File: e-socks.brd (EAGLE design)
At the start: 65.1 x 30 mm, 93 parts, among them IC1 CC2540, IC2 741G240DCK, Q1 FA-20H(32MHz), Q2 ABS06, U2 MAX21000, X4 1296-T10

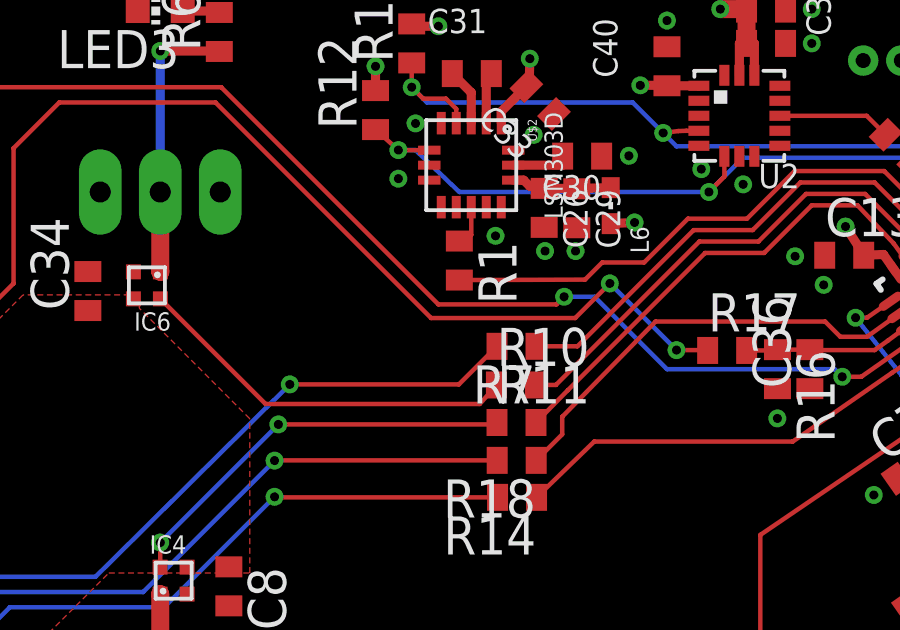
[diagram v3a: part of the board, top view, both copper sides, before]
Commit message: 4K Pulldown Widerstand hinzugefügt, um den Pullup Widerstand im Reset zu überstimmen (nur für 5V-Enable), einige Widerstandswerte angepasst)
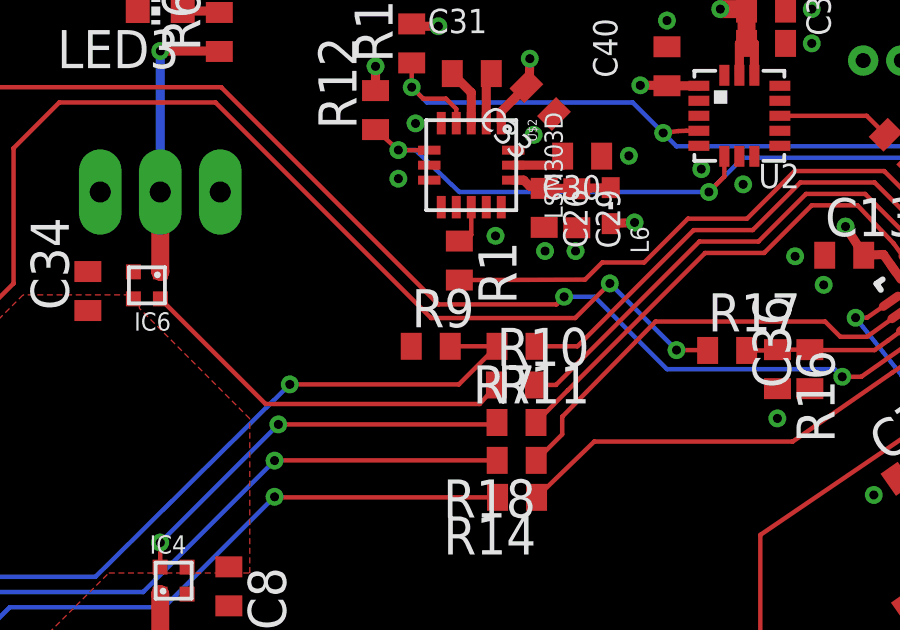
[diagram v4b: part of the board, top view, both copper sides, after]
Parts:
- added R9: 4K, rcl:R0402
- C11: value 100nF -> 220nF
- R16: value 10K -> 24K
- R19: value 4K7 -> 1K2
- R20: value 4K7k -> 1k
- R3: value 47R -> 100k
- R5: value 47R -> 360k
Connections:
- net 5V_ENABLE: now also R9.2
- net GND: now also R9.1
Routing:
- net 5V_ENABLE: track 30.9 -> 32.5 mm
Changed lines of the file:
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@@
 <layer number="20" name="Dimension" color="15" fill="1" visible="yes" active="yes"/>
 <layer number="21" name="tPlace" color="7" fill="1" visible="yes" active="yes"/>
-<layer number="22" name="bPlace" color="7" fill="1" visible="yes" active="yes"/>
+<layer number="22" name="bPlace" color="7" fill="1" visible="no" active="yes"/>
 <layer number="23" name="tOrigins" color="15" fill="1" visible="yes" active="yes"/>
 <layer number="24" name="bOrigins" color="15" fill="1" visible="yes" active="yes"/>
@@
 <element name="R21" library="rcl" package="R0402" value="150K" x="13.02675" y="20.34325" rot="R90"/>
 <element name="R22" library="rcl" package="R0402" value="430K" x="11.88575" y="20.379" rot="R270"/>
-<element name="C11" library="rcl" package="C0402" value="100nF" x="12.016" y="28.0055" rot="R270"/>
-<element name="R20" library="rcl" package="R0402" value="4K7k" x="10.81875" y="28.1405" rot="R90"/>
-<element name="R19" library="rcl" package="R0402" value="4K7" x="9.689" y="27.97925" rot="R90"/>
+<element name="C11" library="rcl" package="C0402" value="220nF" x="12.016" y="28.0055" rot="R270"/>
+<element name="R20" library="rcl" package="R0402" value="1k" x="10.81875" y="28.1405" rot="R90"/>
+<element name="R19" library="rcl" package="R0402" value="1K2" x="9.689" y="27.97925" rot="R90"/>
 <element name="C20" library="resistor" package="C0402" value="2,2µF" x="9.898" y="20.74225" rot="R180"/>
 <element name="R4" library="rcl" package="R0402" value="220R" x="2.555" y="24.06375" rot="MR180"/>
@@
 <element name="R14" library="rcl" package="R0402" value="220R" x="32.784596875" y="12.8719" rot="R180"/>
 <element name="R15" library="rcl" package="R0402" value="47R" x="9.162596875" y="2.17759375"/>
-<element name="R16" library="rcl" package="R0402" value="10K" x="41.4655" y="17.145" rot="R270"/>
+<element name="R16" library="rcl" package="R0402" value="24K" x="41.4655" y="17.145" rot="R270"/>
 <element name="R17" library="rcl" package="R0402" value="10K" x="39.788196875" y="17.76910625"/>
 <element name="C36" library="rcl" package="C0402" value="12pF" x="42.545" y="17.145" rot="R90"/>
@@
 <element name="R18" library="rcl" package="R0402" value="220R" x="32.7737" y="14.1047" rot="R180"/>
 <element name="U$3" library="microusb1" package="MICRO-USB" value="MICRO-USB" x="0" y="24.765" rot="R270"/>
-<element name="R3" library="rcl" package="R0402" value="47R" x="3.683" y="10.541" rot="R180"/>
+<element name="R3" library="rcl" package="R0402" value="100k" x="3.683" y="10.541" rot="R180"/>
 <element name="C2" library="rcl" package="C0603" value="10µF" x="8.636" y="14.351" rot="R90"/>
 <element name="C5" library="rcl" package="C0805" value="22µF" x="10.9855" y="10.7315" rot="R270"/>
 <element name="C6" library="rcl" package="C0805" value="22µF" x="12.8905" y="10.795" rot="R270"/>
-<element name="R5" library="rcl" package="R0402" value="47R" x="4.318" y="8.636" rot="R90"/>
+<element name="R5" library="rcl" package="R0402" value="360k" x="4.318" y="8.636" rot="R90"/>
 <element name="IC4" library="micrel" package="MIC94040" value="" x="21.336" y="10.0965"/>
 <element name="C8" library="rcl" package="C0402" value="1nF" x="23.1775" y="9.906" rot="R270"/>
@@
 <attribute name="MANUFACTURER_PART_NUMBER" value="TL3340AF160QG" x="64.3255" y="26.924" size="1.778" layer="28" rot="MR270" display="off"/>
 </element>
+<element name="R9" library="rcl" package="R0402" value="4K" x="29.9085" y="17.907"/>
 </elements>
 <signals>
@@
 <contactref element="U$1" pad="P5"/>
 <contactref element="U$1" pad="P4"/>
+<contactref element="R9" pad="1"/>
 </signal>
 <signal name="N$28">
@@
 <wire x1="6.085" y1="10.418" x2="5.465" y2="10.418" width="0.254" layer="1"/>
 <wire x1="5.465" y1="10.418" x2="5.2705" y2="10.2235" width="0.254" layer="1"/>
+<contactref element="R9" pad="2"/>
+<wire x1="32.116" y1="17.907" x2="30.5585" y2="17.907" width="0.15" layer="1"/>
 </signal>
 <signal name="N$1">
